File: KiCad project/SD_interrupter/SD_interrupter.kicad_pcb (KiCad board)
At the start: 2 copper layers, 81.3 x 81.3 mm, 37 parts, among them J1 Micro_SD_Card_Det, J2 AVR-ISP-6, J3 DIN-5, SW1 BL_SW, SW2 MAIN_SW, SW3 UP_SW, SW4 DN_SW, SW5 OK_SW, U1 LM7805_TO220, U2 4050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

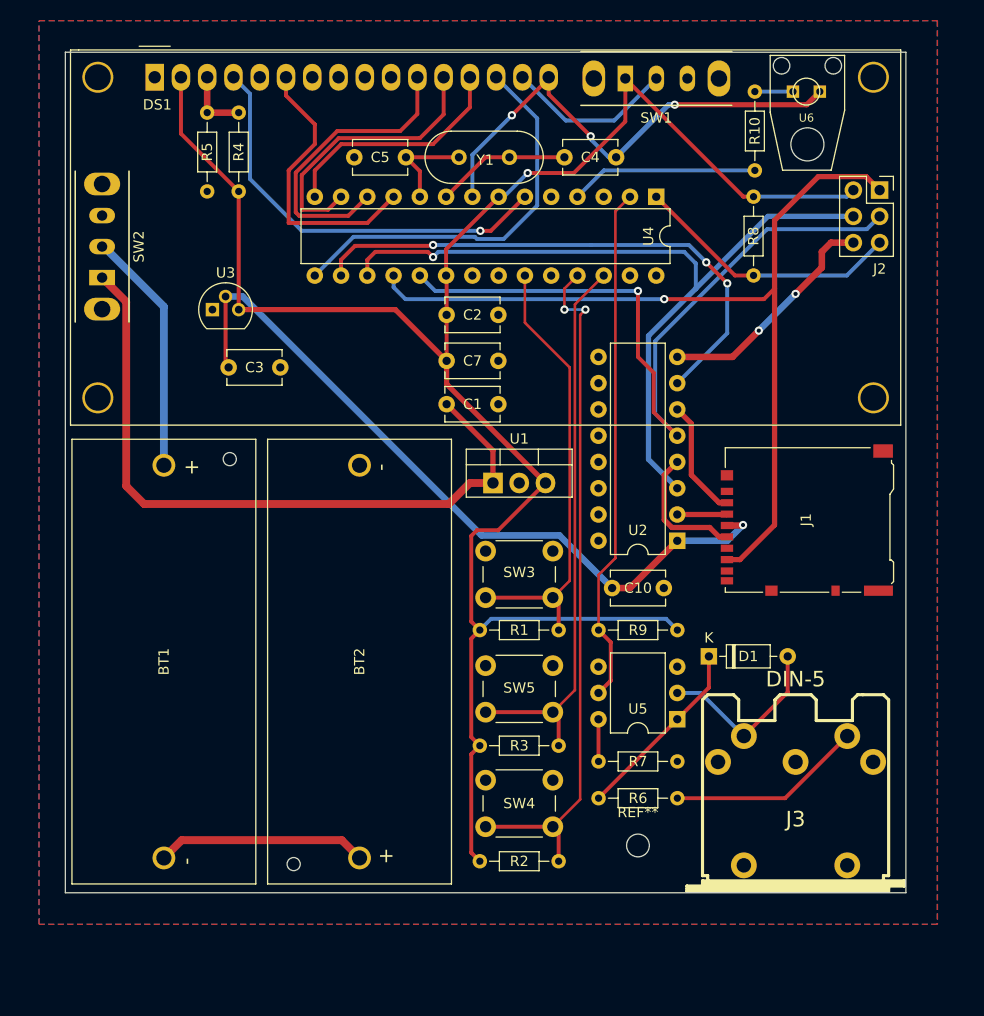
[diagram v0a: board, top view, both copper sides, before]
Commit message: Better PCB routing
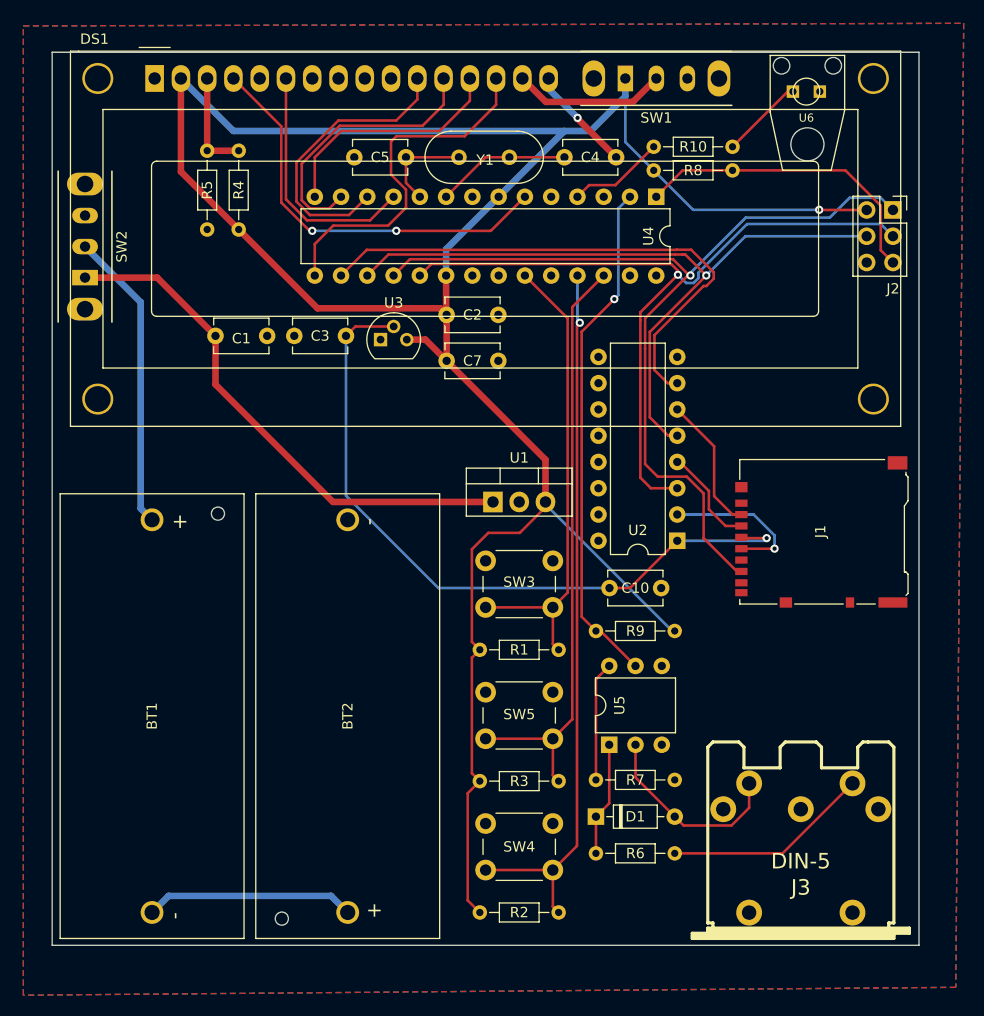
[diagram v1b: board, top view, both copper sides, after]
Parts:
- removed REF**: MountingHole_2.2mm_M2, MountingHole:MountingHole_2.2mm_M2
- moved C1 23.3 mm to (37.4, 52.8)
- moved D1 19.0 mm to (74.2, 99.3)
- moved U3 16.5 mm to (53.3, 53.2)
- moved C3 11.8 mm to (50.0, 52.8), turned to 180 degrees
- moved R10 10.0 mm to (79.8, 34.5), turned to 0 degrees
- moved R8 9.98 mm to (79.8, 36.8), turned to 0 degrees
- moved U5 7.03 mm to (75.5, 92.4), turned to 90 degrees
- moved BT1 5.39 mm to (31.2, 89.6)
- moved BT2 5.39 mm to (50.2, 89.6)
- moved R6 5.34 mm to (81.8, 102.9)
- moved R2 4.95 mm to (62.9, 108.6)
- moved J3 4.60 mm to (94.0, 101.6)
- moved SW4 4.19 mm to (63.5, 100.0)
- moved R4 3.68 mm to (39.6, 34.9)
- moved R5 3.68 mm to (36.6, 34.9)
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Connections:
- J1 pad 3: Net-(J1-Pad3) -> Net-(U2-Pad4)
- U2 pad 2: Net-(J1-Pad3) -> Net-(J1-Pad5)
- U2 pad 3: /DI -> /CLK
- U2 pad 4: Net-(J1-Pad5) -> Net-(U2-Pad4)
- U2 pad 5: /CLK -> /DI
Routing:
- net GND: track 70.3 -> 10.3 mm, vias 5 -> 1
- net +5V: track 189.7 -> 234.4 mm
- net Net-(C1-Pad1): track 67.6 -> 51.2 mm
- net Net-(U2-Pad4): track 0.00 -> 9.81 mm
- net Net-(R10-Pad1): track 18.2 -> 9.38 mm
- net Net-(R7-Pad1): track 4.08 -> 11.6 mm
- net Net-(D1-Pad1): track 18.1 -> 11.0 mm
- net /DI: track 77.4 -> 70.9 mm
- net VCC: track 23.7 -> 29.1 mm
- net Net-(J1-Pad3): track 4.82 -> 0.00 mm
- net /OPT: track 3.68 -> 8.05 mm
- net /RESET: track 26.1 -> 30.2 mm
- net /DB7: track 38.5 -> 34.5 mm
- net /E: track 27.5 -> 23.9 mm
- net Net-(DS1-Pad3): track 6.47 -> 10.0 mm
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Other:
- board size 81.3 x 81.3 mm -> 83.8 x 86.4 mm

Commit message: Minor changes
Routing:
- net +3.3V: track 69.3 -> 58.7 mm, vias 1 -> 0
- net Net-(J1-Pad5): track 14.7 -> 8.45 mm
- net /DO: track 89.8 -> 90.5 mm, vias 1 -> 3
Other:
- board text added: "For private use only"
- board text added: "PCB: Caraffa/Rafal Najda"
- board text added: "Source: OneTesla"
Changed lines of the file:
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@@
       (outputformat 1)
       (mirror false)
-      (drillshape 1)
+      (drillshape 0)
       (scaleselection 1)
-      (outputdirectory "")
+      (outputdirectory "gerbers/")
     )
   )
@@
   )
   (gr_rect (start 21.586 25.4) (end 105.406 111.76) (layer "Edge.Cuts") (width 0.1) (fill none))
+  (gr_text "For private use only" (at 39.624 92.456) (layer "B.SilkS")
+    (effects (font (size 1 1) (thickness 0.15)) (justify mirror))
+  )
+  (gr_text "PCB: Caraffa/Rafal Najda" (at 36.322 90.678) (layer "B.SilkS")
+    (effects (font (size 1 1) (thickness 0.15)) (justify mirror))
+  )
+  (gr_text "Source: OneTesla" (at 40.64 88.646) (layer "B.SilkS")
+    (effects (font (size 1 1) (thickness 0.15)) (justify mirror))
+  )
   (segment (start 32.850685 106.981315) (end 48.561315 106.981315) (width 0.635) (layer "B.Cu") (net 1))
   (segment (start 31.247 108.585) (end 32.850685 106.981315) (width 0.635) (layer "B.Cu") (net 1))
@@
   (segment (start 71.12 33.02) (end 73.66 33.02) (width 0.635) (layer "B.Cu") (net 5))
   (segment (start 81.540981 81.3668) (end 69.29 69.115819) (width 0.254) (layer "B.Cu") (net 5))
-  (segment (start 75.478 77.216) (end 77.46 77.216) (width 0.254) (layer "F.Cu") (net 6))
+  (segment (start 75.478 77.216) (end 77.46 77.216) (width 0.25) (layer "F.Cu") (net 6))
   (segment (start 50.908 51.922) (end 54.61 51.922) (width 0.254) (layer "F.Cu") (net 6))
+  (segment (start 77.46 77.216) (end 82.032 72.644) (width 0.25) (layer "F.Cu") (net 6))
   (segment (start 49.998 52.832) (end 50.908 51.922) (width 0.254) (layer "F.Cu") (net 6))
-  (segment (start 77.46 77.216) (end 82.032 72.644) (width 0.254) (layer "F.Cu") (net 6))
-  (segment (start 88.315 72.39) (end 88.235 72.31) (width 0.254) (layer "F.Cu") (net 6))
-  (segment (start 90.678 72.39) (end 88.315 72.39) (width 0.254) (layer "F.Cu") (net 6))
-  (via (at 90.678 72.39) (size 0.8) (drill 0.4) (layers "F.Cu" "B.Cu") (net 6))
-  (segment (start 82.032 72.644) (end 90.424 72.644) (width 0.254) (layer "B.Cu") (net 6))
-  (segment (start 90.424 72.644) (end 90.678 72.39) (width 0.254) (layer "B.Cu") (net 6))
-  (segment (start 49.998 68.286) (end 49.998 52.832) (width 0.254) (layer "B.Cu") (net 6))
-  (segment (start 75.478 77.216) (end 58.928 77.216) (width 0.254) (layer "B.Cu") (net 6))
-  (segment (start 58.928 77.216) (end 49.998 68.286) (width 0.254) (layer "B.Cu") (net 6))
+  (segment (start 87.901 72.644) (end 88.235 72.31) (width 0.25) (layer "F.Cu") (net 6))
+  (segment (start 82.032 72.644) (end 87.901 72.644) (width 0.25) (layer "F.Cu") (net 6))
+  (segment (start 82.032 72.644) (end 75.537 66.149) (width 0.25) (layer "B.Cu") (net 6))
+  (segment (start 75.537 66.149) (end 63.863 66.149) (width 0.25) (layer "B.Cu") (net 6))
+  (segment (start 54.61 56.896) (end 54.61 51.922) (width 0.25) (layer "B.Cu") (net 6))
+  (segment (start 63.863 66.149) (end 54.61 56.896) (width 0.25) (layer "B.Cu") (net 6))
   (segment (start 65.8 35.56) (end 71.12 35.56) (width 0.254) (layer "F.Cu") (net 7))
   (segment (start 63.5 35.56) (end 59.68 39.38) (width 0.254) (layer "F.Cu") (net 7))
@@
   (segment (start 85.09 67.818) (end 85.09 69.596) (width 0.254) (layer "F.Cu") (net 25))
   (segment (start 82.296 65.024) (end 85.09 67.818) (width 0.254) (layer "F.Cu") (net 25))
-  (segment (start 88.235 73.41) (end 91.436 73.41) (width 0.254) (layer "F.Cu") (net 26))
-  (segment (start 91.436 73.41) (end 91.44 73.406) (width 0.254) (layer "F.Cu") (net 26))
-  (via (at 91.44 73.406) (size 0.8) (drill 0.4) (layers "F.Cu" "B.Cu") (net 26))
-  (segment (start 82.032 70.104) (end 89.420134 70.104) (width 0.254) (layer "B.Cu") (net 26))
-  (segment (start 91.44 72.123866) (end 91.44 73.406) (width 0.254) (layer "B.Cu") (net 26))
-  (segment (start 89.420134 70.104) (end 91.44 72.123866) (width 0.254) (layer "B.Cu") (net 26))
+  (segment (start 85.602 73.41) (end 88.235 73.41) (width 0.25) (layer "F.Cu") (net 26))
+  (segment (start 85.598 73.406) (end 85.602 73.41) (width 0.25) (layer "F.Cu") (net 26))
+  (via (at 85.598 73.406) (size 0.8) (drill 0.4) (layers "F.Cu" "B.Cu") (net 26))
+  (segment (start 82.032 70.104) (end 83.791805 70.104) (width 0.25) (layer "B.Cu") (net 26))
+  (segment (start 83.791805 70.104) (end 85.598 71.910195) (width 0.25) (layer "B.Cu") (net 26))
+  (segment (start 85.598 71.910195) (end 85.598 73.406) (width 0.25) (layer "B.Cu") (net 26))
   (segment (start 78.921 65.224) (end 80.134 66.437) (width 0.254) (layer "F.Cu") (net 27))
   (segment (start 83.192052 46.99) (end 83.312 46.99) (width 0.254) (layer "F.Cu") (net 27))
   (segment (start 83.312 46.99) (end 83.058 46.99) (width 0.254) (layer "F.Cu") (net 27))
   (segment (start 82.947 66.437) (end 84.582 68.072) (width 0.254) (layer "F.Cu") (net 27))
+  (segment (start 84.582 68.072) (end 84.582 71.9195) (width 0.25) (layer "F.Cu") (net 27))
   (segment (start 83.058 46.99) (end 78.921 51.127) (width 0.254) (layer "F.Cu") (net 27))
+  (segment (start 86.36 75.438) (end 88.063 75.438) (width 0.25) (layer "F.Cu") (net 27))
   (segment (start 54.6 47) (end 56.181 45.419) (width 0.254) (layer "F.Cu") (net 27))
   (segment (start 81.621052 45.419) (end 83.192052 46.99) (width 0.254) (layer "F.Cu") (net 27))
-  (segment (start 87.802 75.61) (end 88.235 75.61) (width 0.254) (layer "F.Cu") (net 27))
-  (segment (start 84.582 72.39) (end 87.802 75.61) (width 0.254) (layer "F.Cu") (net 27))
+  (segment (start 88.063 75.438) (end 88.235 75.61) (width 0.25) (layer "F.Cu") (net 27))
   (segment (start 80.134 66.437) (end 82.947 66.437) (width 0.254) (layer "F.Cu") (net 27))
   (segment (start 78.921 51.127) (end 78.921 54.102) (width 0.254) (layer "F.Cu") (net 27))
   (segment (start 78.921 54.036052) (end 78.921 65.224) (width 0.254) (layer "F.Cu") (net 27))
-  (segment (start 84.582 68.072) (end 84.582 72.39) (width 0.254) (layer "F.Cu") (net 27))
   (segment (start 56.181 45.419) (end 81.621052 45.419) (width 0.254) (layer "F.Cu") (net 27))
+  (via (at 86.36 75.438) (size 0.8) (drill 0.4) (layers "F.Cu" "B.Cu") (net 27))
+  (via (at 84.582 71.9195) (size 0.8) (drill 0.4) (layers "F.Cu" "B.Cu") (net 27))
   (via (at 83.312 46.99) (size 0.8) (drill 0.4) (layers "F.Cu" "B.Cu") (net 27))
   (segment (start 83.312 46.736) (end 88.646 41.402) (width 0.254) (layer "B.Cu") (net 27))
@@
   (segment (start 101.713 39.478) (end 102.89 40.655) (width 0.254) (layer "B.Cu") (net 27))
   (segment (start 88.646 41.402) (end 96.774 41.402) (width 0.254) (layer "B.Cu") (net 27))
+  (segment (start 84.582 73.66) (end 86.36 75.438) (width 0.25) (layer "B.Cu") (net 27))
+  (segment (start 84.582 71.9195) (end 84.582 73.66) (width 0.25) (layer "B.Cu") (net 27))
   (segment (start 96.774 41.402) (end 98.698 39.478) (width 0.254) (layer "B.Cu") (net 27))
   (segment (start 82.097598 46.537598) (end 82.097598 46.922974) (width 0.254) (layer "F.Cu") (net 31))
@@
     (polygon
       (pts
-        (xy 108.966 115.824)
-        (xy 18.796 116.586)
-        (xy 18.796 22.86)
-        (xy 109.728 22.606)
+        (xy 108.712 23.622)
+        (xy 108.458 115.062)
+        (xy 18.542 115.57)
+        (xy 19.558 23.114)
       )
     )

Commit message: minor changes
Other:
- board text added: "JLCJLCJLCJLC"
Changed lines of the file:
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@@
     (fp_line (start 68 28) (end -5 28) (layer "F.SilkS") (width 0.12))
     (fp_line (start -8.14 -2.64) (end -8.14 33.64) (layer "F.SilkS") (width 0.12))
-    (fp_arc (start 64.20104 22.49932) (mid 64.054473 22.853115) (end 63.70066 22.9997) (layer "F.SilkS") (width 0.12))
+    (fp_arc (start 64.20104 22.49932) (mid 64.054479 22.85315) (end 63.70066 22.9997) (layer "F.SilkS") (width 0.12))
     (fp_arc (start 0.20066 22.9997) (mid -0.153162 22.853142) (end -0.29972 22.49932) (layer "F.SilkS") (width 0.12))
     (fp_arc (start 63.7 8) (mid 64.053553 8.146447) (end 64.2 8.5) (layer "F.SilkS") (width 0.12))
@@
     (effects (font (size 1 1) (thickness 0.15)) (justify mirror))
   )
+  (gr_text "JLCJLCJLCJLC" (at 30.48 90.678) (layer "F.SilkS")
+    (effects (font (size 1 1) (thickness 0.125)))
+  )
   (segment (start 32.850685 106.981315) (end 48.561315 106.981315) (width 0.635) (layer "B.Cu") (net 1))
